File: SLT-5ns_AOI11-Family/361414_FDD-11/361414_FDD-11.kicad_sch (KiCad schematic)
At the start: 9 parts, among them U1 12-Pin_SLx_Can

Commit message: Updated schematics
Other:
- note removed: "B"
- note removed: "C"
- note removed: "E"
- note removed: "Transistor Die Layout (top view)"
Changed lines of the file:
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@@
     (stroke (width 0) (type default) (color 0 0 0 0))
-  )
-  (polyline (pts (xy 252.73 29.21) (xy 252.73 40.64))
-    (stroke (width 0) (type solid) (color 0 0 0 0))
   )
   (wire (pts (xy 96.52 80.01) (xy 104.14 80.01))
     (stroke (width 0) (type default) (color 0 0 0 0))
-  )
-  (polyline (pts (xy 264.16 40.64) (xy 252.73 40.64))
-    (stroke (width 0) (type solid) (color 0 0 0 0))
   )
   (wire (pts (xy 137.16 106.68) (xy 137.16 101.6))
@@
     (stroke (width 0) (type default) (color 0 0 0 0))
   )
-  (polyline (pts (xy 252.73 29.21) (xy 264.16 29.21))
-    (stroke (width 0) (type solid) (color 0 0 0 0))
-  )
   (wire (pts (xy 104.14 106.68) (xy 104.14 101.6))
     (stroke (width 0) (type default) (color 0 0 0 0))
-  )
-  (polyline (pts (xy 264.16 29.21) (xy 264.16 40.64))
-    (stroke (width 0) (type solid) (color 0 0 0 0))
   )
   (wire (pts (xy 152.4 101.6) (xy 137.16 101.6))
@@
     (stroke (width 0) (type default) (color 0 0 0 0))
   )
-  (text "C" (at 257.81 39.37 0)
-    (effects (font (size 1.27 1.27)) (justify left bottom))
-  )
   (text "All Diodes DC" (at 114.3 57.15 0)
     (effects (font (size 1.27 1.27)) (justify left bottom))
   )
-  (text "E" (at 254 33.02 0)
-    (effects (font (size 1.27 1.27)) (justify left bottom))
-  )
-  (text "B" (at 261.62 33.02 0)
-    (effects (font (size 1.27 1.27)) (justify left bottom))
-  )
-  (text "Transistor Die Layout (top view)" (at 243.84 27.94 0)
-    (effects (font (size 1.27 1.27)) (justify left bottom))
-  )

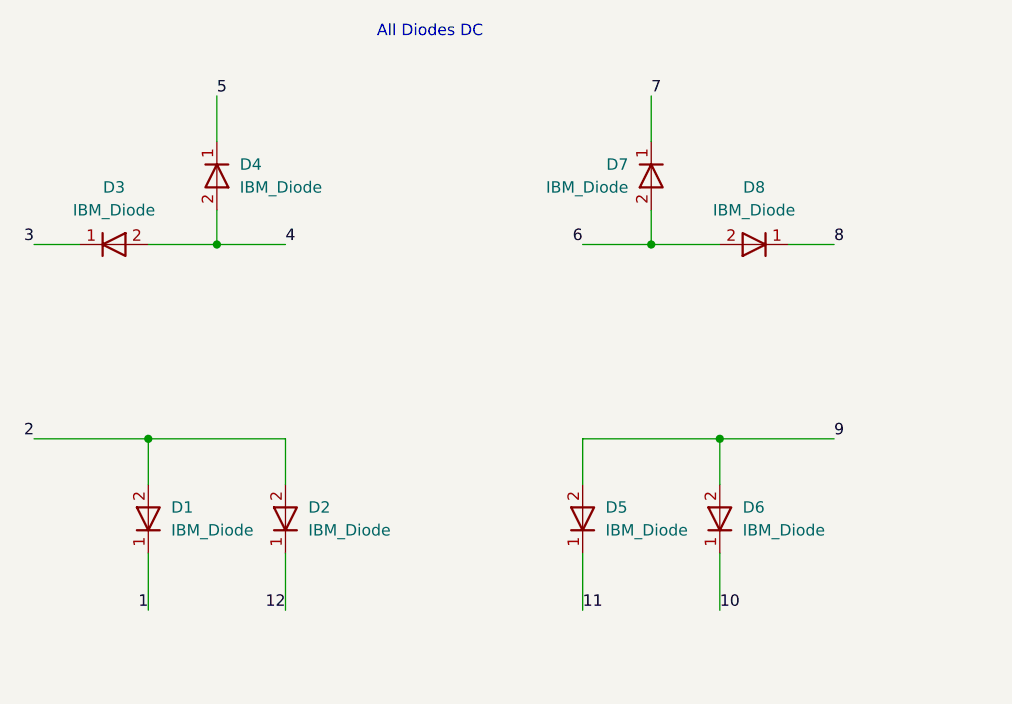
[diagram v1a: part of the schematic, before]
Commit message: Finished off the SLT-30 family of parts, started on the SLT-700 family. Changed labeling of transistors and diodes in all schematics, but have yet to update all the pdf files. This is a TODO...
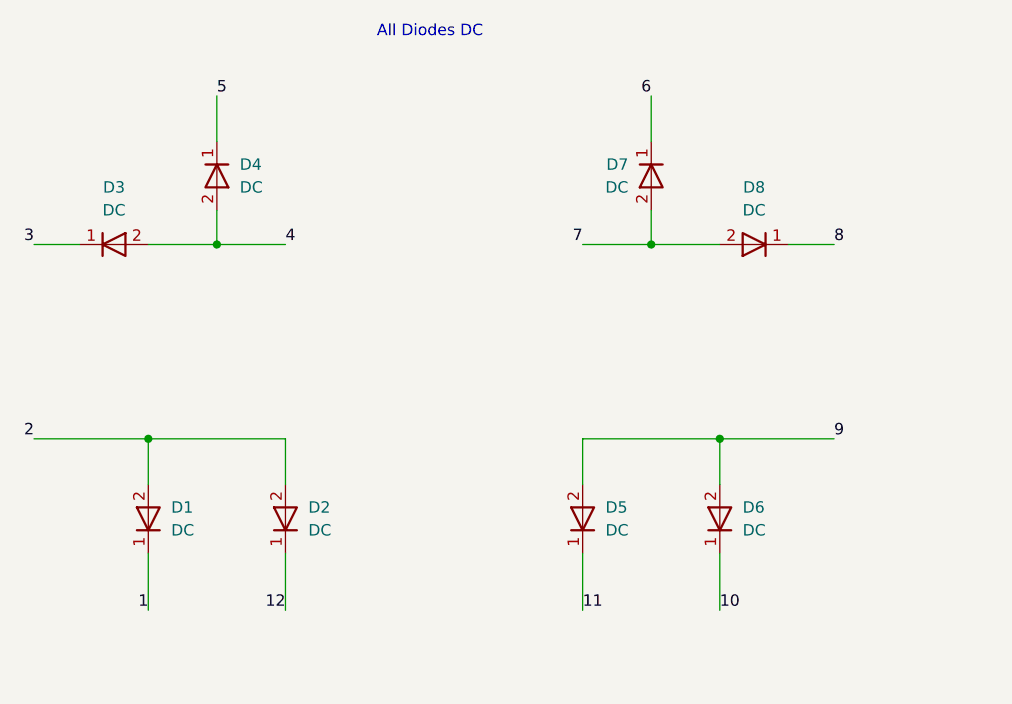
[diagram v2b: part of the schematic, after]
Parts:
- D1, D2, D3, D4, D5, D6, D7, D8: value IBM_Diode -> DC
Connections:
- net 6: now also D7.1 (K); no longer D7.2 (A), D8.2 (A)
- net 7: now also D7.2 (A), D8.2 (A); no longer D7.1 (K)
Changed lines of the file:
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@@
     (effects (font (size 1.27 1.27)) (justify left bottom))
   )
-  (label "6" (at 137.16 80.01 180)
+  (label "6" (at 144.78 63.5 180)
     (effects (font (size 1.27 1.27)) (justify right bottom))
   )
@@
     (effects (font (size 1.27 1.27)) (justify right bottom))
   )
-  (label "7" (at 144.78 63.5 0)
-    (effects (font (size 1.27 1.27)) (justify left bottom))
+  (label "7" (at 137.16 80.01 180)
+    (effects (font (size 1.27 1.27)) (justify right bottom))
   )
   (label "3" (at 76.2 80.01 180)
@@
       (effects (font (size 1.27 1.27)) (justify left))
     )
-    (property "Value" "IBM_Diode" (id 1) (at 99.06 73.6599 90)
+    (property "Value" "DC" (id 1) (at 99.06 73.6599 90)
       (effects (font (size 1.27 1.27)) (justify left))
     )
@@
       (effects (font (size 1.27 1.27)) (justify right))
     )
-    (property "Value" "IBM_Diode" (id 1) (at 106.68 111.7599 90)
+    (property "Value" "DC" (id 1) (at 106.68 111.7599 90)
       (effects (font (size 1.27 1.27)) (justify right))
     )
@@
       (effects (font (size 1.27 1.27)) (justify left))
     )
-    (property "Value" "IBM_Diode" (id 1) (at 142.24 73.6599 90)
+    (property "Value" "DC" (id 1) (at 142.24 73.6599 90)
       (effects (font (size 1.27 1.27)) (justify left))
     )
@@
       (effects (font (size 1.27 1.27)) (justify right))
     )
-    (property "Value" "IBM_Diode" (id 1) (at 91.44 111.7599 90)
+    (property "Value" "DC" (id 1) (at 91.44 111.7599 90)
       (effects (font (size 1.27 1.27)) (justify right))
     )
@@
     (in_bom yes) (on_board yes) (fields_autoplaced)
     (property "Reference" "D8" (id 0) (at 156.21 73.66 0))
-    (property "Value" "IBM_Diode" (id 1) (at 156.21 76.2 0))
+    (property "Value" "DC" (id 1) (at 156.21 76.2 0))
     (property "Footprint" "Diode_SMD:D_0201_0603Metric" (id 2) (at 156.21 82.55 0)
       (effects (font (size 1.27 1.27)) hide)
@@
     (in_bom yes) (on_board yes) (fields_autoplaced)
     (property "Reference" "D3" (id 0) (at 85.09 73.66 0))
-    (property "Value" "IBM_Diode" (id 1) (at 85.09 76.2 0))
+    (property "Value" "DC" (id 1) (at 85.09 76.2 0))
     (property "Footprint" "Diode_SMD:D_0201_0603Metric" (id 2) (at 85.09 77.47 0)
       (effects (font (size 1.27 1.27)) hide)
@@
       (effects (font (size 1.27 1.27)) (justify right))
     )
-    (property "Value" "IBM_Diode" (id 1) (at 139.7 111.7599 90)
+    (property "Value" "DC" (id 1) (at 139.7 111.7599 90)
       (effects (font (size 1.27 1.27)) (justify right))
     )
@@
       (effects (font (size 1.27 1.27)) (justify right))
     )
-    (property "Value" "IBM_Diode" (id 1) (at 154.94 111.7599 90)
+    (property "Value" "DC" (id 1) (at 154.94 111.7599 90)
       (effects (font (size 1.27 1.27)) (justify right))
     )
@@
   (symbol_instances
     (path "/801d24ff-be6b-468d-a51b-7691568aa1d6"
-      (reference "D1") (unit 1) (value "IBM_Diode") (footprint "Diode_SMD:D_0201_0603Metric")
+      (reference "D1") (unit 1) (value "DC") (footprint "Diode_SMD:D_0201_0603Metric")
     )
     (path "/15a433c4-0335-46e4-884c-814357806383"
-      (reference "D2") (unit 1) (value "IBM_Diode") (footprint "Diode_SMD:D_0201_0603Metric")
+      (reference "D2") (unit 1) (value "DC") (footprint "Diode_SMD:D_0201_0603Metric")
     )
     (path "/b60d9340-c16c-48dd-8b20-3b5943f6c8ab"
-      (reference "D3") (unit 1) (value "IBM_Diode") (footprint "Diode_SMD:D_0201_0603Metric")
+      (reference "D3") (unit 1) (value "DC") (footprint "Diode_SMD:D_0201_0603Metric")
     )
     (path "/096216c5-6902-43a5-8004-8a4114c8baa4"
-      (reference "D4") (unit 1) (value "IBM_Diode") (footprint "Diode_SMD:D_0201_0603Metric")
+      (reference "D4") (unit 1) (value "DC") (footprint "Diode_SMD:D_0201_0603Metric")
     )
     (path "/e1f12525-18b0-44bc-a18d-820be7b9946e"
-      (reference "D5") (unit 1) (value "IBM_Diode") (footprint "Diode_SMD:D_0201_0603Metric")
+      (reference "D5") (unit 1) (value "DC") (footprint "Diode_SMD:D_0201_0603Metric")
     )
     (path "/e5207290-41d1-4708-be96-2b2603b0ffee"
-      (reference "D6") (unit 1) (value "IBM_Diode") (footprint "Diode_SMD:D_0201_0603Metric")
+      (reference "D6") (unit 1) (value "DC") (footprint "Diode_SMD:D_0201_0603Metric")
     )
     (path "/1be5506a-07a3-447d-b379-4e04e402bbb9"
-      (reference "D7") (unit 1) (value "IBM_Diode") (footprint "Diode_SMD:D_0201_0603Metric")
+      (reference "D7") (unit 1) (value "DC") (footprint "Diode_SMD:D_0201_0603Metric")
     )
     (path "/8e4b9e6c-d9b9-437f-9616-3123e2a2c38e"
-      (reference "D8") (unit 1) (value "IBM_Diode") (footprint "Diode_SMD:D_0201_0603Metric")
+      (reference "D8") (unit 1) (value "DC") (footprint "Diode_SMD:D_0201_0603Metric")
     )
     (path "/75e072b9-86c1-407b-a1c4-16b7a7044004"
